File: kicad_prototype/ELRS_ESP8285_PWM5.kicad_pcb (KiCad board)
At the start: 4 copper layers, 17.5 x 24.5 mm, 54 parts, among them J1 Conn_Coaxial, J2 Conn_01x05, J3 Conn_01x05, J4 Conn_01x05, J5 Conn_Coaxial, J6 Conn_01x02, U1 SPX3819M5-L-3-3, U2 ESP8285, U5 2450FM07D0034T, U6 SX1281, Y2 26M, Y3 52M

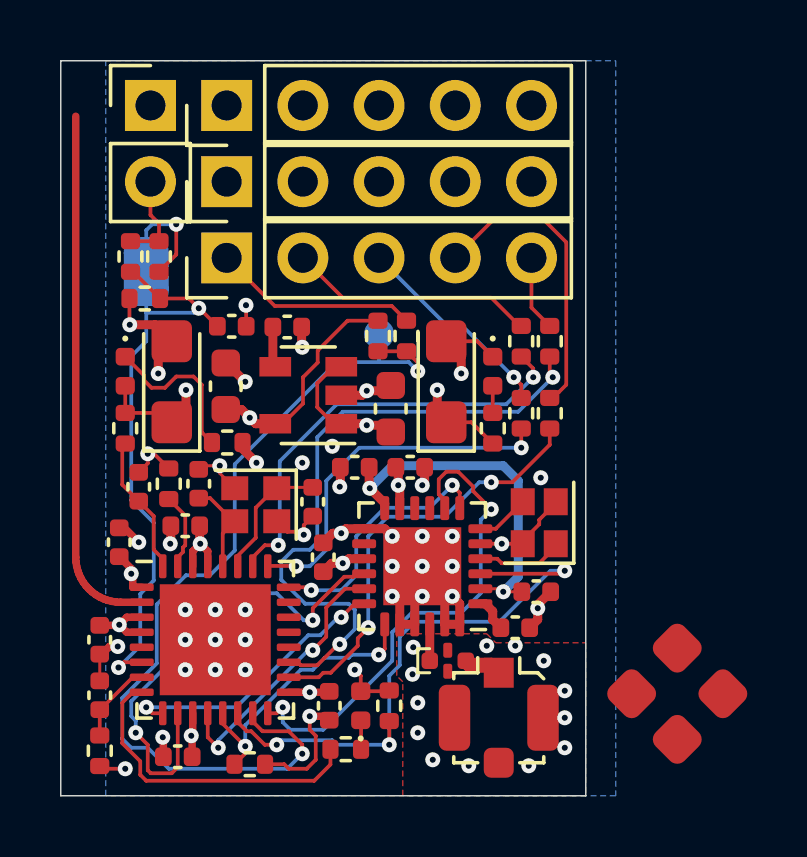
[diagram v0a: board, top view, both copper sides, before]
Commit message: add series cap to antenna trace
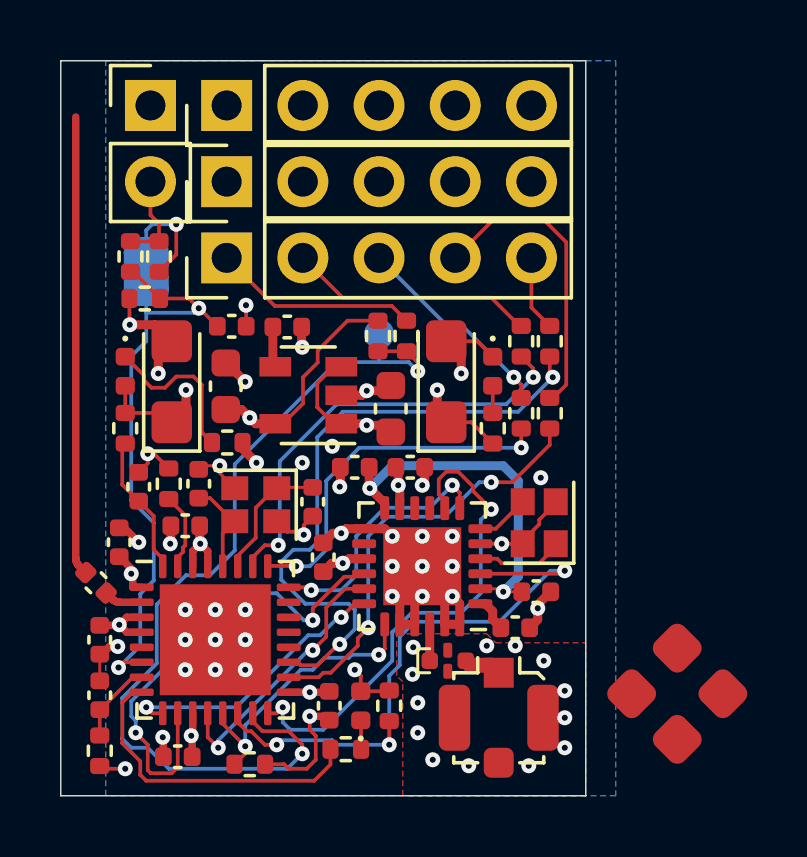
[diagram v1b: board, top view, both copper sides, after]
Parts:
- added C13: 10p, Capacitor_SMD:C_0402_1005Metric, F.Cu at (159.2, 68.4)
- JP1: value SolderJumper_2_Bridged -> 6S4S
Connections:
- U2 pad 2: ANT -> Net-(C13-Pad2)
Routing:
- net ANT: track 17.8 -> 15.3 mm
- net Net-(C13-Pad2): track 0.00 -> 1.30 mm
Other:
- board text added: "crteensy rev0.4"
- board text removed: "crteensy rev0.3"

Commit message: update rev0.6
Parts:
- D1: value LED -> blue_2V9
- D2: value LED -> true_gr_3V3
- D4: value LED -> red_2V1
- JP1: value 6S4S -> 4S; footprint Jumper:SolderJumper-2_P1.3mm_Bridged_RoundedPad1.0x1.5mm -> Jumper:SolderJumper-2_P1.3mm_Open_RoundedPad1.0x1.5mm
- R11: value 560R -> 270R
- R12: value 3k9 -> 4k7
- moved TP1 1.11 mm to (167.5, 60.1)
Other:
- board text added: "1"
- board text added: "2 Tx"
- board text added: "3 Rx"
- board text added: "4"
- board text added: "4S"
- board text added: "5"
- board text added: "B"
- board text added: "GVS"
- board text added: "crteensy ELRS 8285 1280 PWM rev0.6"
- board text removed: "Boot"
- board text removed: "crteensy rev0.4"

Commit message: general update
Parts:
- added TP2: TestPoint, TestPoint:TestPoint_Pad_D1.0mm, B.Cu at (162.0, 60.5)
- C19, C20: value 5p -> 4p7
- TP1: value BOOT -> TestPoint
- moved TP1 6.21 mm to (162.0, 63.0)
- turned D4 to -90 degrees
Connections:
- D4 pad 1: Net-(D4-Pad1) -> GND
- D4 pad 2: +3V3 -> Net-(D4-Pad2)
- R4 pad 2: Net-(D4-Pad1) -> Net-(D4-Pad2)
- TP1 pad 1: PWM1 -> +3V3
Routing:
- net GND: track 44.8 -> 46.8 mm, vias 55 -> 63
- net Net-(J3-Pad2): track 8.28 -> 9.92 mm
- net Net-(D4-Pad2): track 0.00 -> 0.97 mm
- net Net-(D4-Pad1): track 0.97 -> 0.00 mm
- net PWM1: track 30.7 -> 29.7 mm
- net NRST_A: track 19.6 -> 20.2 mm
- net +3V3: track 25.9 -> 26.5 mm
- added copper zone on In1.Cu, net +3V3
- added copper zone on In1.Cu, net +5V
- added copper zone on In2.Cu, net GND
- removed copper zone on In1.Cu_3V3, net +3V3
- removed copper zone on In1.Cu_3V3, net +5V
- removed copper zone on In2.Cu_Gnd, net GND
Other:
- net class Default removed
- board text added: "3V3"
- board text added: "crteensy ELRS 8285 1280 PWM rev1.0"
- board text removed: "B"
- board text removed: "crteensy ELRS 8285 1280 PWM rev0.6"
